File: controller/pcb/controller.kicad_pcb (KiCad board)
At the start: 2 copper layers, 89.1 x 49.9 mm, 28 parts, among them J1 Conn_01x10_Pin, SW1 SW_Push, SW2 SW_Push, SW3 SW_Push, SW4 SW_Push, U1 COM-09032, U2 COM-09032, U3 NRF24L01_Breakout, U4 ESP32C3-SUPERMINI, U5 74HC148

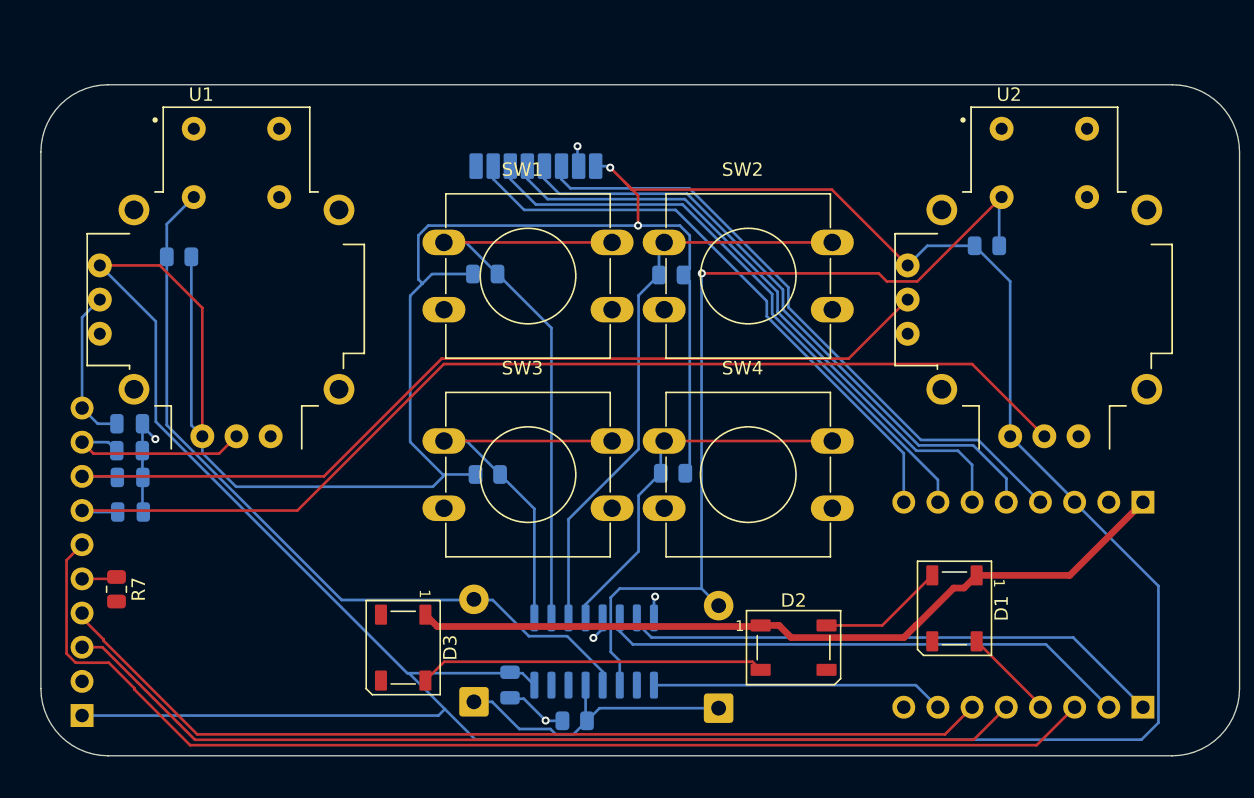
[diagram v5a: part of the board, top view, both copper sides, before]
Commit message: [pcb] change footprint for joystick on controller
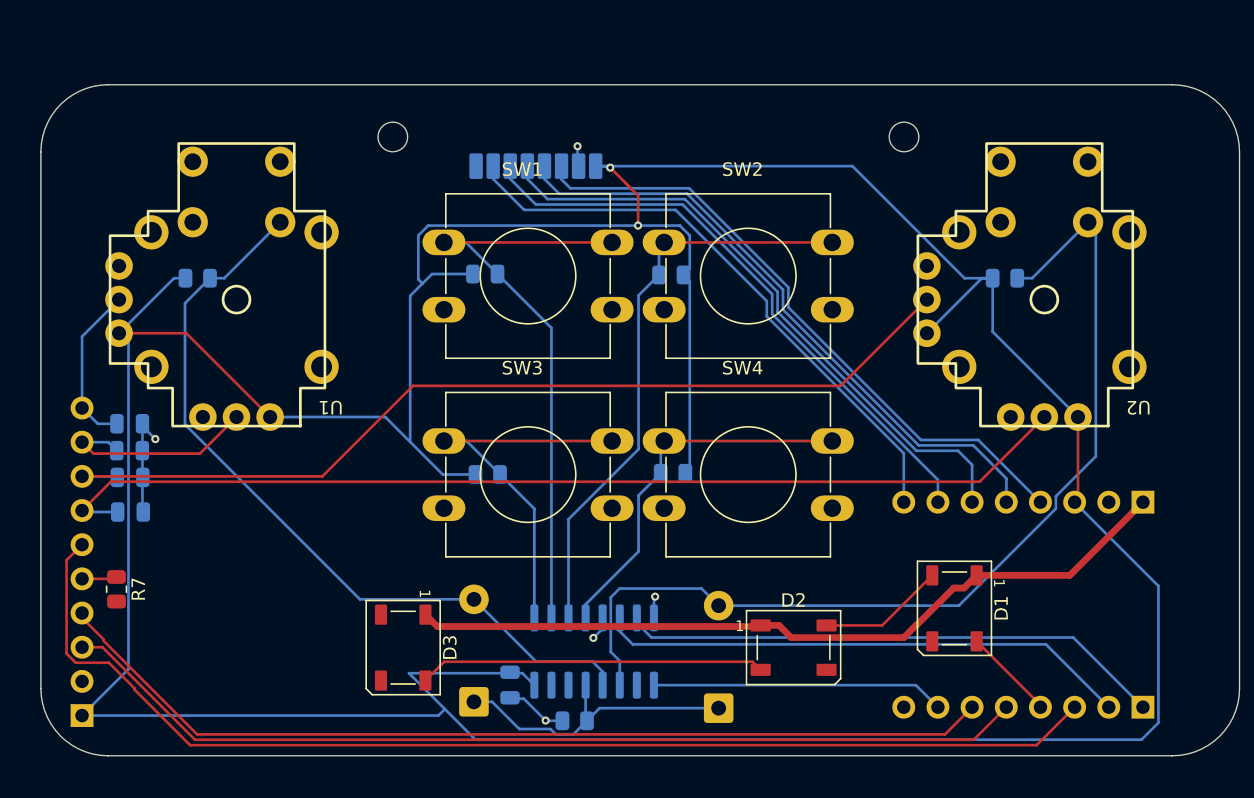
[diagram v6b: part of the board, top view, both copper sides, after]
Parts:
- added REF**: MountingHole_2.2mm_M2, MountingHole:MountingHole_2.2mm_M2, F.Cu at (127.5, 55.5)
- added REF**: MountingHole_2.2mm_M2, MountingHole:MountingHole_2.2mm_M2, F.Cu at (165.5, 55.5)
- U1, U2: value COM-09032 -> PS5; footprint stuff:XDCR_COM-09032 -> stuff:Joystick
- moved R6 2.76 mm to (173.0, 66.0)
- moved R5 2.11 mm to (113.0, 66.0), turned to 180 degrees
- turned U1 to 180 degrees
- turned U2 to 180 degrees
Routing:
- net +3.3V: track 329.9 -> 306.6 mm
- net BTN_JOY_R: track 67.9 -> 73.4 mm, vias 1 -> 0
- net JOY2_H: track 81.0 -> 77.1 mm
- net JOY2_V: track 69.5 -> 70.9 mm
- net JOY1_V: track 11.7 -> 12.3 mm
- net JOY1_H: track 15.2 -> 15.8 mm
- net BTN_JOY_L: track 58.8 -> 58.2 mm

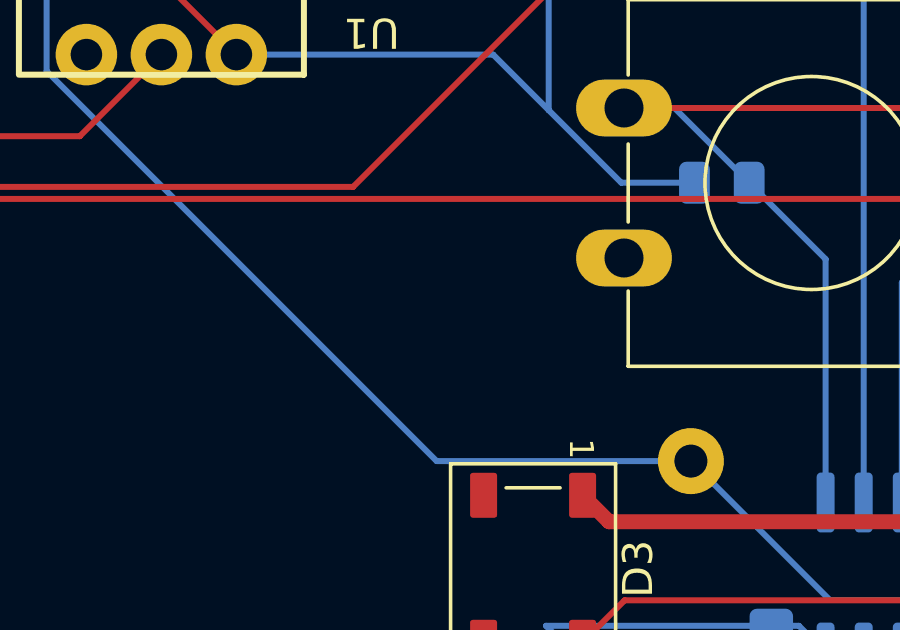
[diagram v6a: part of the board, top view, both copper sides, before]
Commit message: [pcb] add additional mounting hole for controller
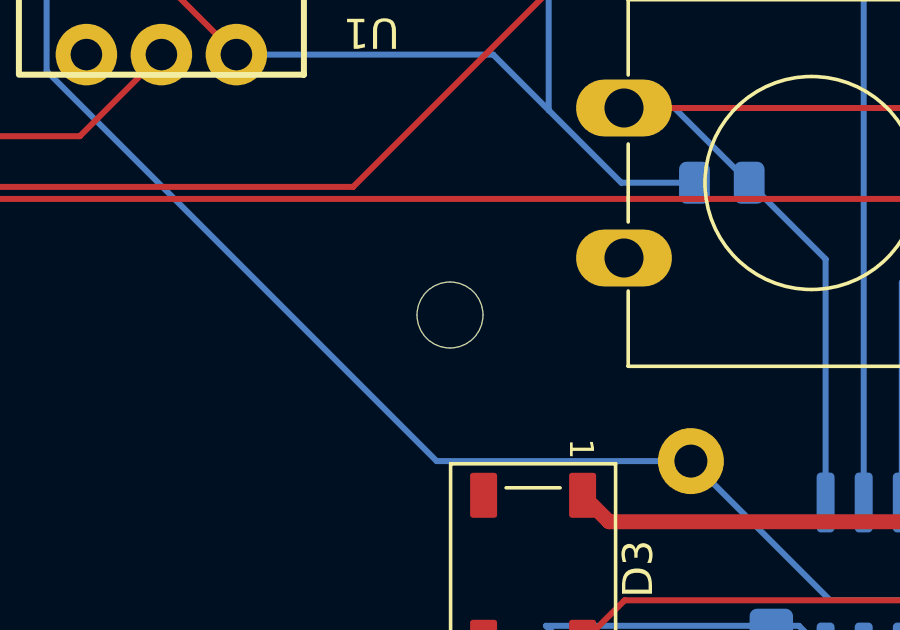
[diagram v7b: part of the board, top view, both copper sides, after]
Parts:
- added REF**: MountingHole_2.2mm_M2, MountingHole:MountingHole_2.2mm_M2, F.Cu at (125.5, 85.0)
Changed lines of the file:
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@@
 		)
+	)
+	(footprint "MountingHole:MountingHole_2.2mm_M2"
+		(layer "F.Cu")
+		(at 125.5 85)
+		(descr "Mounting Hole 2.2mm, M2, no annular, generated by kicad-footprint-generator mountinghole.py")
+		(tags "mountinghole M2")
+		(property "Reference" "REF**"
+			(at 0 -3.15 0)
+			(layer "F.SilkS")
+			(hide yes)
+			(effects
+				(font
+					(size 1 1)
+					(thickness 0.15)
+				)
+			)
+		)
+		(property "Value" "MountingHole_2.2mm_M2"
+			(at 0 3.15 0)
+			(layer "F.Fab")
+			(hide yes)
+			(effects
+				(font
+					(size 1 1)
+					(thickness 0.15)
+				)
+			)
+		)
+		(property "Datasheet" ""
+			(at 0 0 0)
+			(layer "F.Fab")
+			(hide yes)
+			(effects
+				(font
+					(size 1.27 1.27)
+					(thickness 0.15)
+				)
+			)
+		)
+		(property "Description" ""
+			(at 0 0 0)
+			(layer "F.Fab")
+			(hide yes)
+			(effects
+				(font
+					(size 1.27 1.27)
+					(thickness 0.15)
+				)
+			)
+		)
+		(attr board_only exclude_from_pos_files exclude_from_bom)
+		(fp_circle
+			(center 0 0)
+			(end 2.2 0)
+			(stroke
+				(width 0.15)
+				(type solid)
+			)
+			(fill no)
+			(layer "Cmts.User")
+		)
+		(fp_circle
+			(center 0 0)
+			(end 2.45 0)
+			(stroke
+				(width 0.05)
+				(type solid)
+			)
+			(fill no)
+			(layer "F.CrtYd")
+		)
+		(fp_text user "${REFERENCE}"
+			(at 0 0 0)
+			(layer "F.Fab")
+			(effects
+				(font
+					(size 1 1)
+					(thickness 0.15)
+				)
+			)
+		)
+		(pad "" np_thru_hole circle
+			(at 0 0)
+			(size 2.2 2.2)
+			(drill 2.2)
+			(layers "*.Cu" "*.Mask")
+		)
+		(embedded_fonts no)
 	)
 	(footprint "LED_SMD:LED_WS2812B_PLCC4_5.0x5.0mm_P3.2mm"
